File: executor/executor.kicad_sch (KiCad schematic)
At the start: 134 parts, among them J1 XT30PW(2+2), J2 gh1.25, 3p, Q1 WNM6006, Q2 WNM6006, Q3 WNM6006, Q4 WNM6006, Q5 WNM6006, Q6 WNM6006, U1 WD1601E, U2 DRV8323SRTAT, U3 GD32F303RETx, U4 TCAN4550RGYRQ1, U5 AS5047P-ATSM, U6 QMA7981, Y1 8M, Y2 40M

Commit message: [New] Fix position for executor
Signed-off-by: Homalozoa <nx.tardis@gmail.com>
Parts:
- removed C22: 47uF, 10% 50V, Capacitor_SMD:CP_Elec_8x6.2, symbol Device:C_Polarized_US
- removed R38: 120R, Resistor_SMD:R_0402_1005Metric, symbol Device:R_US
- Y1, Y2: footprint Oscillator:Oscillator_SMD_EuroQuartz_XO32-4Pin_3.2x2.5mm -> Oscillator:Oscillator_SMD_ECS_2520MV-xxx-xx-4Pin_2.5x2.0mm
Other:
- moved on the sheet: D3
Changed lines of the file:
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@@
   (junction (at 506.73 361.95) (diameter 0) (color 0 0 0 0)
   )
-  (junction (at 514.35 339.09) (diameter 0) (color 0 0 0 0)
-  )
   (junction (at 176.53 64.77) (diameter 0) (color 0 0 0 0)
   )
   (junction (at 80.01 349.25) (diameter 0) (color 0 0 0 0)
   )
-  (junction (at 115.57 158.75) (diameter 0) (color 0 0 0 0)
-  )
   (junction (at 113.03 288.29) (diameter 0) (color 0 0 0 0)
   )
@@
   (junction (at 156.21 195.58) (diameter 0) (color 0 0 0 0)
   )
-  (junction (at 115.57 128.27) (diameter 0) (color 0 0 0 0)
-  )
   (junction (at 60.96 128.27) (diameter 0) (color 0 0 0 0)
   )
@@
   (junction (at 166.37 64.77) (diameter 0) (color 0 0 0 0)
   )
-  (junction (at 532.13 351.79) (diameter 0) (color 0 0 0 0)
-  )
   (junction (at 181.61 346.71) (diameter 0) (color 0 0 0 0)
   )
@@
   (junction (at 129.54 346.71) (diameter 0) (color 0 0 0 0)
   )
-  (junction (at 151.13 128.27) (diameter 0) (color 0 0 0 0)
+  (junction (at 119.38 128.27) (diameter 0) (color 0 0 0 0)
   )
   (junction (at 439.42 302.26) (diameter 0) (color 0 0 0 0)
@@
     (stroke (width 0) (type default) (color 0 0 0 0))
   )
-  (wire (pts (xy 115.57 158.75) (xy 152.4 158.75))
-    (stroke (width 0) (type default) (color 0 0 0 0))
-  )
   (wire (pts (xy 449.58 210.82) (xy 449.58 226.06))
     (stroke (width 0) (type default) (color 0 0 0 0))
@@
     (stroke (width 0) (type default) (color 0 0 0 0))
   )
-  (wire (pts (xy 115.57 128.27) (xy 115.57 137.16))
-    (stroke (width 0) (type default) (color 0 0 0 0))
-  )
   (wire (pts (xy 110.49 77.47) (xy 114.3 77.47))
     (stroke (width 0) (type default) (color 0 0 0 0))
@@
     (stroke (width 0) (type default) (color 0 0 0 0))
   )
-  (wire (pts (xy 532.13 339.09) (xy 532.13 341.63))
-    (stroke (width 0) (type default) (color 0 0 0 0))
-  )
   (wire (pts (xy 524.51 143.51) (xy 524.51 147.32))
     (stroke (width 0) (type default) (color 0 0 0 0))
@@
     (stroke (width 0) (type default) (color 0 0 0 0))
   )
-  (wire (pts (xy 514.35 339.09) (xy 532.13 339.09))
-    (stroke (width 0) (type default) (color 0 0 0 0))
-  )
   (wire (pts (xy 236.22 314.96) (xy 236.22 320.04))
     (stroke (width 0) (type default) (color 0 0 0 0))
@@
     (stroke (width 0) (type default) (color 0 0 0 0))
   )
-  (wire (pts (xy 151.13 128.27) (xy 151.13 142.24))
+  (wire (pts (xy 119.38 128.27) (xy 119.38 142.24))
     (stroke (width 0) (type default) (color 0 0 0 0))
   )
@@
     (stroke (width 0) (type default) (color 0 0 0 0))
   )
-  (wire (pts (xy 152.4 158.75) (xy 152.4 149.86))
+  (wire (pts (xy 120.65 158.75) (xy 120.65 149.86))
     (stroke (width 0) (type default) (color 0 0 0 0))
   )
@@
     (stroke (width 0) (type default) (color 0 0 0 0))
   )
-  (wire (pts (xy 153.67 128.27) (xy 153.67 142.24))
+  (wire (pts (xy 121.92 128.27) (xy 121.92 142.24))
     (stroke (width 0) (type default) (color 0 0 0 0))
   )
@@
     (stroke (width 0) (type default) (color 0 0 0 0))
   )
-  (wire (pts (xy 151.13 128.27) (xy 153.67 128.27))
+  (wire (pts (xy 119.38 128.27) (xy 121.92 128.27))
     (stroke (width 0) (type default) (color 0 0 0 0))
   )
@@
     (stroke (width 0) (type default) (color 0 0 0 0))
   )
-  (wire (pts (xy 115.57 128.27) (xy 151.13 128.27))
-    (stroke (width 0) (type default) (color 0 0 0 0))
-  )
   (wire (pts (xy 88.9 349.25) (xy 80.01 349.25))
     (stroke (width 0) (type default) (color 0 0 0 0))
   )
-  (wire (pts (xy 109.22 128.27) (xy 115.57 128.27))
+  (wire (pts (xy 109.22 128.27) (xy 119.38 128.27))
     (stroke (width 0) (type default) (color 0 0 0 0))
   )
@@
     (stroke (width 0) (type default) (color 0 0 0 0))
   )
-  (wire (pts (xy 115.57 144.78) (xy 115.57 158.75))
-    (stroke (width 0) (type default) (color 0 0 0 0))
-  )
   (wire (pts (xy 137.16 229.87) (xy 137.16 232.41))
     (stroke (width 0) (type default) (color 0 0 0 0))
@@
     (stroke (width 0) (type default) (color 0 0 0 0))
   )
-  (wire (pts (xy 109.22 158.75) (xy 115.57 158.75))
+  (wire (pts (xy 109.22 158.75) (xy 120.65 158.75))
     (stroke (width 0) (type default) (color 0 0 0 0))
   )
@@
     (stroke (width 0) (type default) (color 0 0 0 0))
   )
-  (wire (pts (xy 532.13 349.25) (xy 532.13 351.79))
-    (stroke (width 0) (type default) (color 0 0 0 0))
-  )
   (wire (pts (xy 303.53 372.11) (xy 302.26 372.11))
     (stroke (width 0) (type default) (color 0 0 0 0))
@@
     (property "Reference" "Y1" (id 0) (at 292.1 172.72 0))
     (property "Value" "8M" (id 1) (at 299.72 172.72 0))
-    (property "Footprint" "Oscillator:Oscillator_SMD_EuroQuartz_XO32-4Pin_3.2x2.5mm" (id 2) (at 295.91 177.8 0)
+    (property "Footprint" "Oscillator:Oscillator_SMD_ECS_2520MV-xxx-xx-4Pin_2.5x2.0mm" (id 2) (at 295.91 177.8 0)
       (effects (font (size 1.27 1.27)) hide)
     )
@@
     (pin "1")
   )
-  (symbol (lib_id "Device:C_Polarized_US") (at 115.57 140.97 0) (unit 1)
-    (in_bom yes) (on_board yes) (fields_autoplaced)
-    (property "Reference" "C22" (id 0) (at 119.38 139.0649 0)
-      (effects (font (size 1.27 1.27)) (justify left))
-    )
-    (property "Value" "47uF, 10% 50V" (id 1) (at 119.38 141.6049 0)
-      (effects (font (size 1.27 1.27)) (justify left))
-    )
-    (property "Footprint" "Capacitor_SMD:CP_Elec_8x6.2" (id 2) (at 115.57 140.97 0)
-      (effects (font (size 1.27 1.27)) hide)
-    )
-    (property "Datasheet" "~" (id 3) (at 115.57 140.97 0)
-      (effects (font (size 1.27 1.27)) hide)
-    )
-    (pin "1")
-    (pin "2")
-  )
   (symbol (lib_id "Device:C") (at 469.9 322.58 0) (unit 1)
     (in_bom yes) (on_board yes)
@@
     (pin "1")
   )
-  (symbol (lib_id "Device:R_US") (at 532.13 345.44 180) (unit 1)
-    (in_bom yes) (on_board yes) (fields_autoplaced)
-    (property "Reference" "R38" (id 0) (at 529.59 346.7101 0)
-      (effects (font (size 1.27 1.27)) (justify left))
-    )
-    (property "Value" "120R" (id 1) (at 529.59 344.1701 0)
-      (effects (font (size 1.27 1.27)) (justify left))
-    )
-    (property "Footprint" "Resistor_SMD:R_0402_1005Metric" (id 2) (at 531.114 345.186 90)
-      (effects (font (size 1.27 1.27)) hide)
-    )
-    (property "Datasheet" "~" (id 3) (at 532.13 345.44 0)
-      (effects (font (size 1.27 1.27)) hide)
-    )
-    (pin "1")
-    (pin "2")
-  )
   (symbol (lib_id "power:+24V") (at 114.3 45.72 0) (unit 1)
     (in_bom yes) (on_board yes) (fields_autoplaced)
@@
     (property "Reference" "Y2" (id 0) (at 425.45 297.18 0))
     (property "Value" "40M" (id 1) (at 433.07 297.18 0))
-    (property "Footprint" "Oscillator:Oscillator_SMD_EuroQuartz_XO32-4Pin_3.2x2.5mm" (id 2) (at 429.26 302.26 0)
+    (property "Footprint" "Oscillator:Oscillator_SMD_ECS_2520MV-xxx-xx-4Pin_2.5x2.0mm" (id 2) (at 429.26 302.26 0)
       (effects (font (size 1.27 1.27)) hide)
     )
@@
     (pin "2")
   )
-  (symbol (lib_id "Rolling_Custom:ESD56161D30") (at 152.4 146.05 270) (unit 1)
+  (symbol (lib_id "Rolling_Custom:ESD56161D30") (at 120.65 146.05 270) (unit 1)
     (in_bom yes) (on_board yes) (fields_autoplaced)
-    (property "Reference" "D3" (id 0) (at 154.94 144.4624 90)
+    (property "Reference" "D3" (id 0) (at 123.19 144.4624 90)
       (effects (font (size 1.27 1.27)) (justify left))
     )
-    (property "Value" "ESD56161D30" (id 1) (at 154.94 147.0024 90)
+    (property "Value" "ESD56161D30" (id 1) (at 123.19 147.0024 90)
       (effects (font (size 1.27 1.27)) (justify left))
     )
-    (property "Footprint" "Rolling_Custom:DFN2x2-3L" (id 2) (at 152.4 146.05 0)
+    (property "Footprint" "Rolling_Custom:DFN2x2-3L" (id 2) (at 120.65 146.05 0)
       (effects (font (size 1.27 1.27)) hide)
     )
-    (property "Datasheet" "" (id 3) (at 152.4 146.05 0)
+    (property "Datasheet" "" (id 3) (at 120.65 146.05 0)
       (effects (font (size 1.27 1.27)) hide)
     )
@@
       (reference "C21") (unit 1) (value "10uF, 20%, 50V") (footprint "Capacitor_SMD:C_0805_2012Metric")
     )
-    (path "/2d312449-bd2d-45db-af0a-0ab2430b325b"
-      (reference "C22") (unit 1) (value "47uF, 10% 50V") (footprint "Capacitor_SMD:CP_Elec_8x6.2")
-    )
     (path "/a6390892-27d7-4d6c-a7b1-a3b09ce43b73"
       (reference "C23") (unit 1) (value "100nF, 10%, 50V") (footprint "Capacitor_SMD:C_0402_1005Metric")
@@
       (reference "R37") (unit 1) (value "2.2k, 5%") (footprint "Resistor_SMD:R_0402_1005Metric")
     )
-    (path "/79afe85b-226b-422d-8602-a7c42d6793f3"
-      (reference "R38") (unit 1) (value "120R") (footprint "Resistor_SMD:R_0402_1005Metric")
-    )
     (path "/33d510f7-a429-47bc-862f-6ce59a537880"
       (reference "TP1") (unit 1) (value "3V3") (footprint "TestPoint:TestPoint_Pad_D2.0mm")
@@
     )
     (path "/111ae7f0-9d94-47d2-9252-a39a462bcbd1"
-      (reference "Y1") (unit 1) (value "8M") (footprint "Oscillator:Oscillator_SMD_EuroQuartz_XO32-4Pin_3.2x2.5mm")
+      (reference "Y1") (unit 1) (value "8M") (footprint "Oscillator:Oscillator_SMD_ECS_2520MV-xxx-xx-4Pin_2.5x2.0mm")
     )
     (path "/7d925c5d-5f91-46c5-884d-15b3ccd597fd"
-      (reference "Y2") (unit 1) (value "40M") (footprint "Oscillator:Oscillator_SMD_EuroQuartz_XO32-4Pin_3.2x2.5mm")
+      (reference "Y2") (unit 1) (value "40M") (footprint "Oscillator:Oscillator_SMD_ECS_2520MV-xxx-xx-4Pin_2.5x2.0mm")
     )
   )

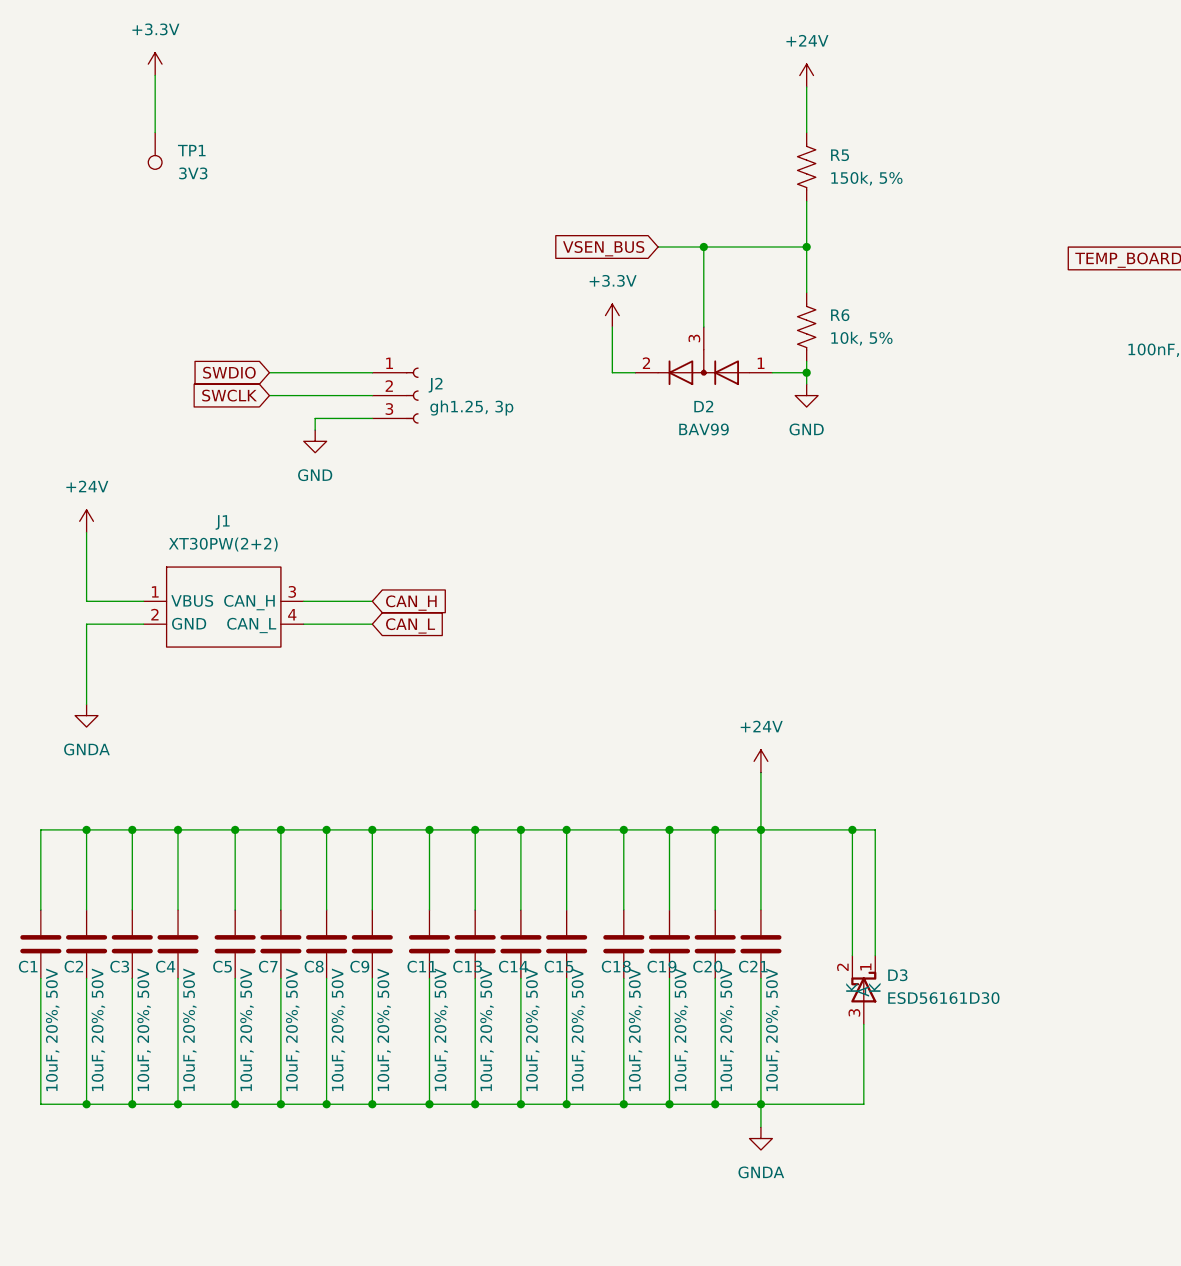
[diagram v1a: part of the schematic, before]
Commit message: [New] Add 4pin for fast flash
Signed-off-by: Homalozoa <nx.tardis@gmail.com>
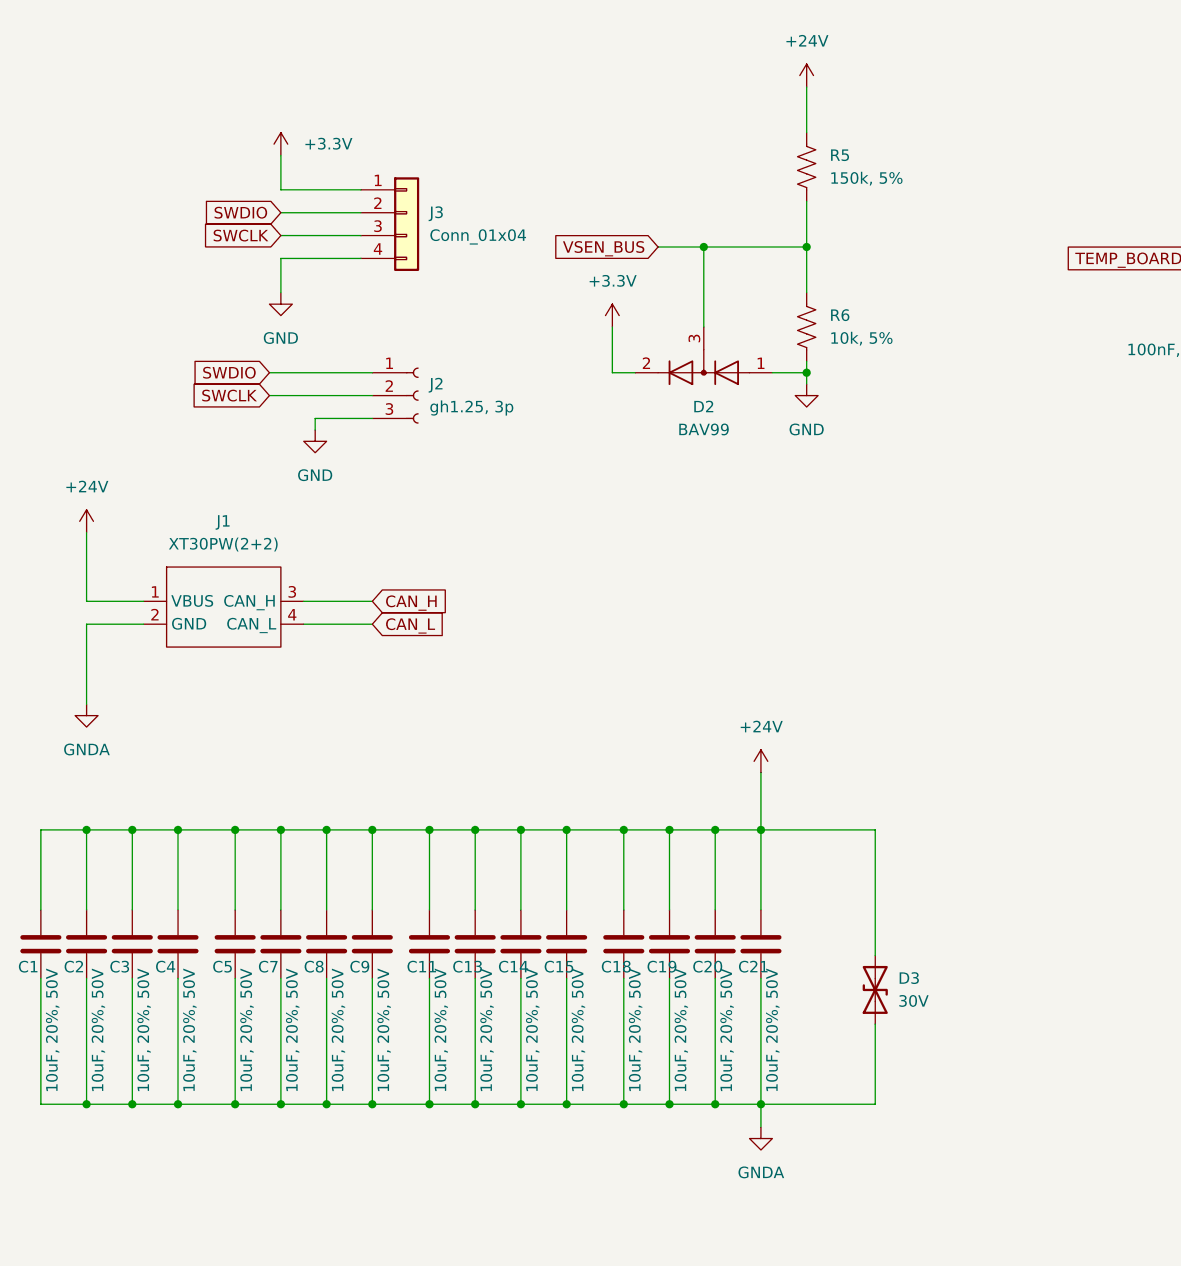
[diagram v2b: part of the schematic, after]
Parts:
- removed D3: ESD56161D30, Rolling_Custom:DFN2x2-3L, symbol Rolling_Custom:ESD56161D30
- removed TP1: 3V3, TestPoint:TestPoint_Pad_D2.0mm, symbol Connector:TestPoint
- added D3: 30V, Diode_SMD:D_SMA, symbol Device:D_TVS
- added J3: Conn_01x04, Connector_PinHeader_1.27mm:PinHeader_1x04_P1.27mm_Vertical, symbol Connector_Generic:Conn_01x04
- TP13, TP14: footprint TestPoint:TestPoint_Loop_D1.80mm_Drill1.0mm_Beaded -> TestPoint:TestPoint_THTPad_D1.0mm_Drill0.5mm
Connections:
- net +24V: now also D3.2 (A2)
- net +3V3: now also J3.1 (Pin_1)
- net GND: now also J3.4 (Pin_4)
- net GNDA: now also D3.1 (A1)
- net SWCLK: now also J3.3 (Pin_3)
- net SWDIO: now also J3.2 (Pin_2)
